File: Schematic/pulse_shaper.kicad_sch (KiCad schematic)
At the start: 48 parts, among them J1 Conn_Coaxial, J2 Conn_Coaxial, J3 Conn_Coaxial, J4 Conn_Coaxial, J5 Conn_Coaxial, J6 Conn_Coaxial, U3 ADA4898-2, U4 ADA4898-2, U5 ADA4898-2, U6 ADA4898-2, U7 ADA4898-2, U8 ADA4898-2

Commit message: Add footprint to components
Added footprint and 3D models to most of the component.
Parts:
- removed U3, U4, U5, U6, U7, U8: ADA4898-2, Package_SO:SOIC-8-1EP_3.9x4.9mm_P1.27mm_EP2.41x3.81mm, symbol Amplifier_Operational:ADA4898-2
- added U3, U4, U5, U6, U7, U8: ADA4891-2ARZ-R7, ADA4891-2ARZ-R7:SOIC8, symbol ADA4891-2ARZ-R7:ADA4891-2ARZ-R7
- R10, R11, R13, R14, R15, R16, R17, R18, R19, R2, R20, R21, R23, R25, R26, R27, R28, R29, R3, R30, R31, R32, R33, R36, R37, R4, R5, R7, R8, R9: footprint (none) -> Resistor_THT:R_Axial_DIN0309_L9.0mm_D3.2mm_P12.70mm_Horizontal
- R12, R22, R24, R34, R35, R6: footprint (none) -> Potentiometer_THT:Potentiometer_Bourns_3266Y_Vertical
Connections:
- net 3V3: now also U3.P$8, U4.P$8, U5.P$8, U6.P$8, U7.P$8, U8.P$8
- net GND: now also U3.P$4, U4.P$4, U5.P$4, U6.P$4, U7.P$4, U8.P$4
- net pulse_in1: now also U3.P$3
- net pulse_in2: now also U4.P$3
- net pulse_in3: now also U5.P$3
- net pulse_in4: now also U6.P$3
- net pulse_in5: now also U7.P$3
- net pulse_in6: now also U8.P$3
- net pulse_out1: now also U3.P$7
- net pulse_out2: now also U4.P$7
- net pulse_out3: now also U5.P$7
- net pulse_out4: now also U6.P$7
- net pulse_out5: now also U7.P$7
- net pulse_out6: now also U8.P$7
- net at R29.2, R31.1: now also U8.P$1
- net at R27.2, R29.1: now also U8.P$2
- net at R18.2, R23.1: now also U6.P$5
- net at R19.2, R22.1: now also U6.P$6
- net at R15.2, R17.1: now also U5.P$2
- net at R21.2, R24.1: now also U5.P$6
- net at R10.2, R13.1: now also U4.P$5
- net at R11.2, R12.1: now also U4.P$6
- net at R20.2, R25.1: now also U5.P$5
- net at R17.2, R20.1: now also U5.P$1
- net at R33.2, R35.1: now also U8.P$6
- net at R8.2, R9.1: now also U4.P$2
- net at R14.2, R16.1: now also U6.P$2
- net at R16.2, R18.1: now also U6.P$1
- net at R2.2, R3.1: now also U3.P$2
- net at R3.2, R4.1: now also U3.P$1
- net at R4.2, R7.1: now also U3.P$5
- net at R5.2, R6.1: now also U3.P$6
- net at R26.2, R28.1: now also U7.P$2
- net at R32.2, R34.1: now also U7.P$6
- net at R31.2, R37.1: now also U8.P$5
- net at R30.2, R36.1: now also U7.P$5
- net at R10.1, R9.2: now also U4.P$1
- net at R28.2, R30.1: now also U7.P$1

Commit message: fix nucleo footprint
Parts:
- U3, U4, U5, U6, U7, U8: footprint ADA4891-2ARZ-R7:SOIC8 -> ADA4891:SOIC8
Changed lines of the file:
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@@
 			)
 		)
-		(property "Footprint" "ADA4891-2ARZ-R7:SOIC8"
+		(property "Footprint" "ADA4891:SOIC8"
 			(at 87.63 210.82 0)
 			(effects
@@
 			)
 		)
-		(property "Footprint" "ADA4891-2ARZ-R7:SOIC8"
+		(property "Footprint" "ADA4891:SOIC8"
 			(at 49.53 167.64 0)
 			(effects
@@
 			)
 		)
-		(property "Footprint" "ADA4891-2ARZ-R7:SOIC8"
+		(property "Footprint" "ADA4891:SOIC8"
 			(at 88.9 170.18 0)
 			(effects
@@
 			)
 		)
-		(property "Footprint" "ADA4891-2ARZ-R7:SOIC8"
+		(property "Footprint" "ADA4891:SOIC8"
 			(at 49.53 120.65 0)
 			(effects
@@
 			)
 		)
-		(property "Footprint" "ADA4891-2ARZ-R7:SOIC8"
+		(property "Footprint" "ADA4891:SOIC8"
 			(at 48.26 255.27 0)
 			(effects
@@
 			)
 		)
-		(property "Footprint" "ADA4891-2ARZ-R7:SOIC8"
+		(property "Footprint" "ADA4891:SOIC8"
 			(at 92.71 29.21 0)
 			(effects
@@
 			)
 		)
-		(property "Footprint" "ADA4891-2ARZ-R7:SOIC8"
+		(property "Footprint" "ADA4891:SOIC8"
 			(at 88.9 76.2 0)
 			(effects
@@
 			)
 		)
-		(property "Footprint" "ADA4891-2ARZ-R7:SOIC8"
+		(property "Footprint" "ADA4891:SOIC8"
 			(at 88.9 123.19 0)
 			(effects
@@
 			)
 		)
-		(property "Footprint" "ADA4891-2ARZ-R7:SOIC8"
+		(property "Footprint" "ADA4891:SOIC8"
 			(at 53.34 26.67 0)
 			(effects
@@
 			)
 		)
-		(property "Footprint" "ADA4891-2ARZ-R7:SOIC8"
+		(property "Footprint" "ADA4891:SOIC8"
 			(at 87.63 257.81 0)
 			(effects
@@
 			)
 		)
-		(property "Footprint" "ADA4891-2ARZ-R7:SOIC8"
+		(property "Footprint" "ADA4891:SOIC8"
 			(at 49.53 73.66 0)
 			(effects
@@
 			)
 		)
-		(property "Footprint" "ADA4891-2ARZ-R7:SOIC8"
+		(property "Footprint" "ADA4891:SOIC8"
 			(at 48.26 208.28 0)
 			(effects

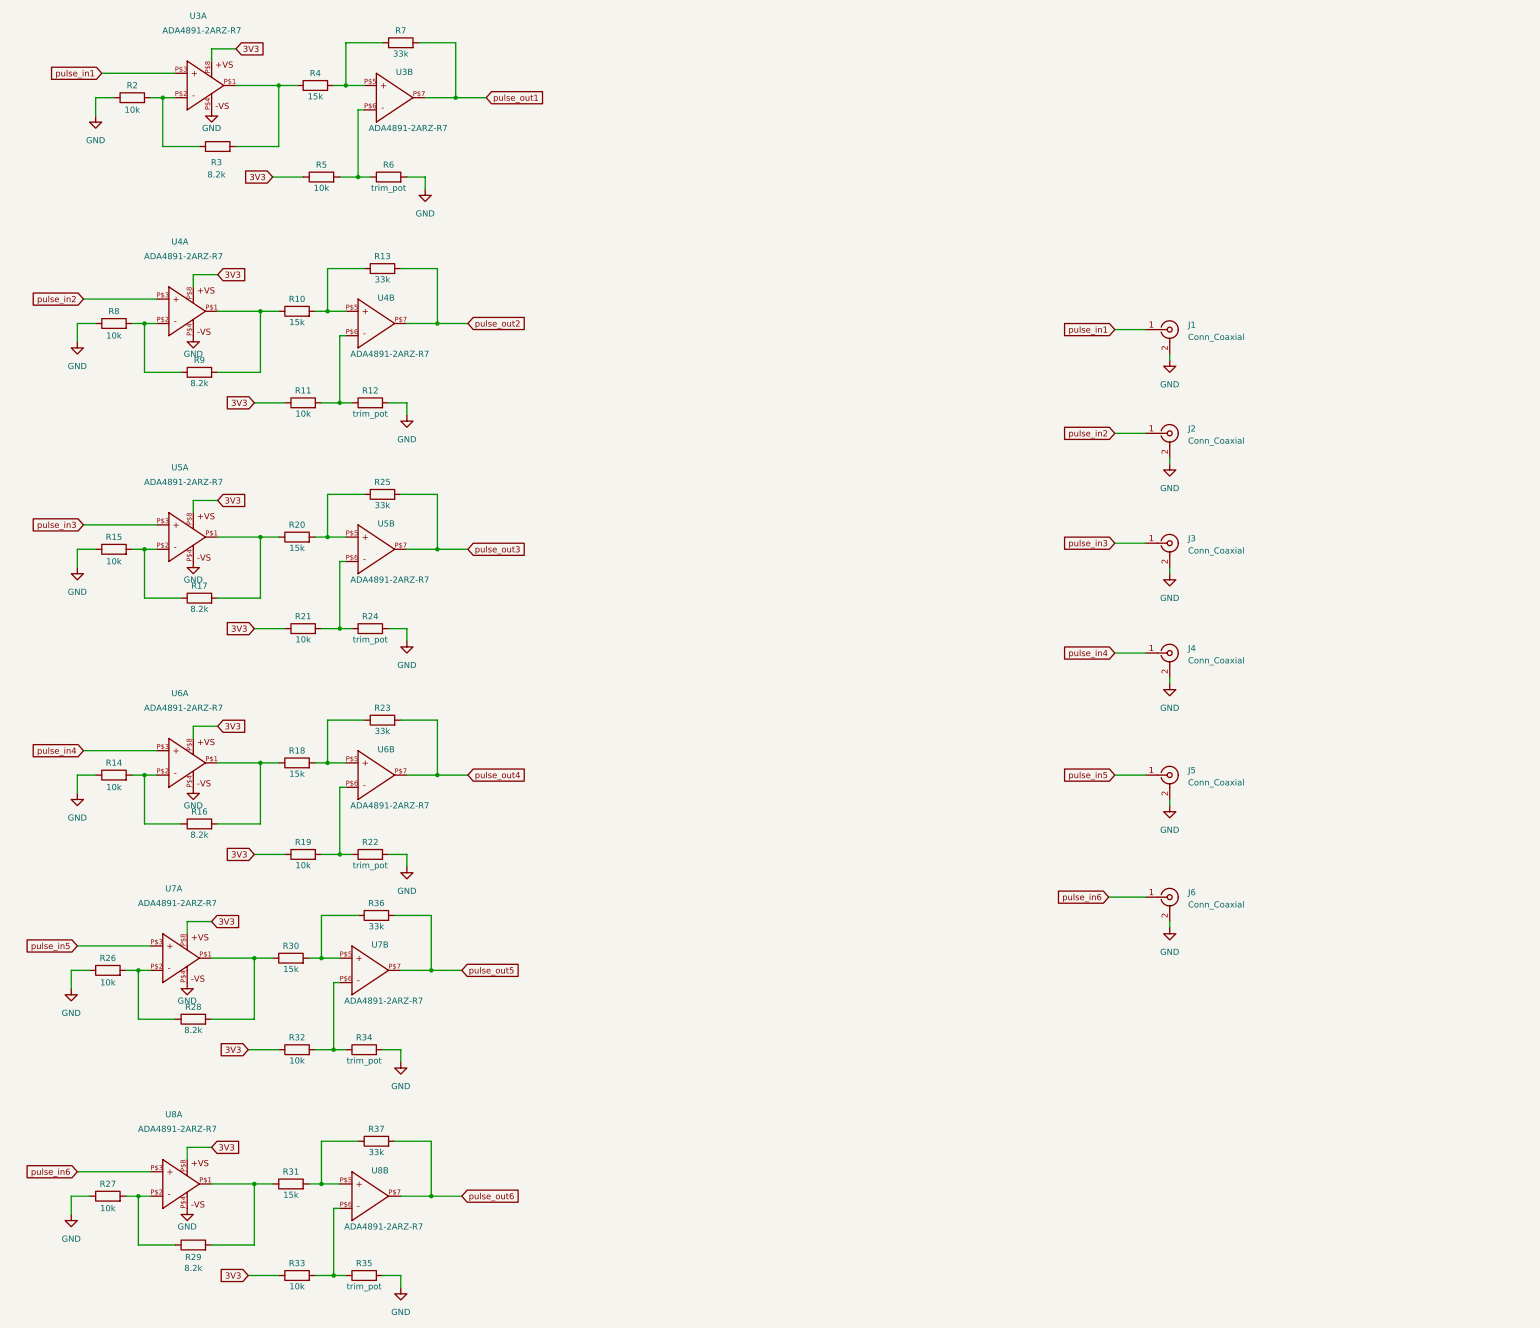
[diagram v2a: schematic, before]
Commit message: fix schematic and pcb layout
Fix Potentiometer errors, and updated schematic
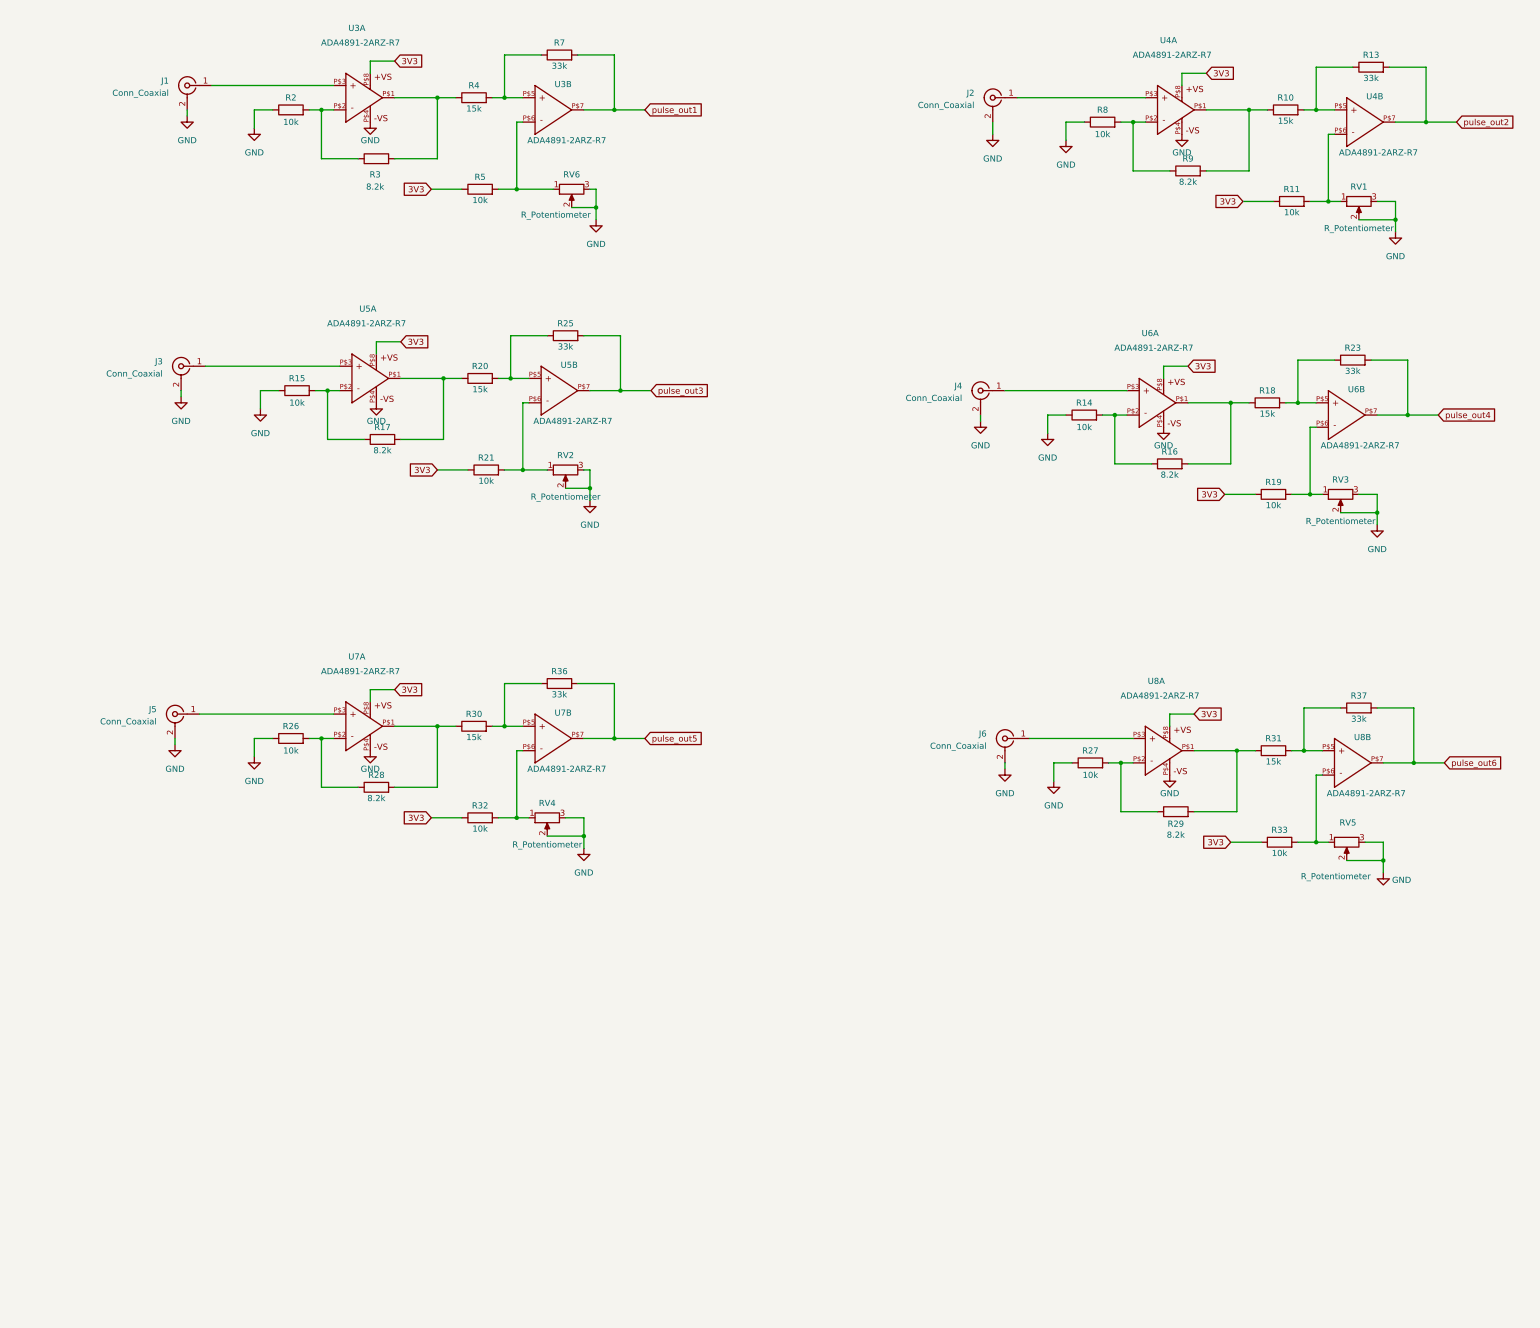
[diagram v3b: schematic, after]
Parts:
- removed R12, R22, R24, R34, R35, R6: trim_pot, Potentiometer_THT:Potentiometer_Bourns_3266Y_Vertical, symbol Device:R
- added RV1, RV2, RV3, RV4, RV5, RV6: R_Potentiometer, Potentiometer_THT:Potentiometer_Bourns_3299Y_Vertical, symbol Device:R_Potentiometer
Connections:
- net GND: now also RV1.2, RV1.3, RV2.2, RV2.3, RV3.2, RV3.3, RV4.2, RV4.3, RV5.2, RV5.3, RV6.2, RV6.3
- net at R32.2, U7.P$6: now also RV4.1
- net at R21.2, U5.P$6: now also RV2.1
- net at R11.2, U4.P$6: now also RV1.1
- net at R19.2, U6.P$6: now also RV3.1
- net at R33.2, U8.P$6: now also RV5.1
- net at R5.2, U3.P$6: now also RV6.1
- net pulse_in1: no longer names the net of J1.1 (In), U3.P$3
- net pulse_in2: no longer names the net of J2.1 (In), U4.P$3
- net pulse_in3: no longer names the net of J3.1 (In), U5.P$3
- net pulse_in4: no longer names the net of J4.1 (In), U6.P$3
- net pulse_in5: no longer names the net of J5.1 (In), U7.P$3
- net pulse_in6: no longer names the net of J6.1 (In), U8.P$3
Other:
- moved on the sheet: J1, J2, J3, J4, J5, J6, R10, R11, R13, R14, R15, R16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

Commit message: update
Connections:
- net GND: now also RV4.1; no longer RV4.3
- net at R32.2, U7.P$6: now also RV4.3; no longer RV4.1
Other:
- moved on the sheet: RV4
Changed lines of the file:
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@@
 	(symbol
 		(lib_id "Device:R_Potentiometer")
-		(at 125.73 179.07 90)
-		(mirror x)
+		(at 125.73 179.07 270)
 		(unit 1)
 		(exclude_from_sim no)
